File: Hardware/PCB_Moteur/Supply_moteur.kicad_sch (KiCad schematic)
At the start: 26 parts, among them J1 Vin_XT30PW-F, U1 L6981N33DR

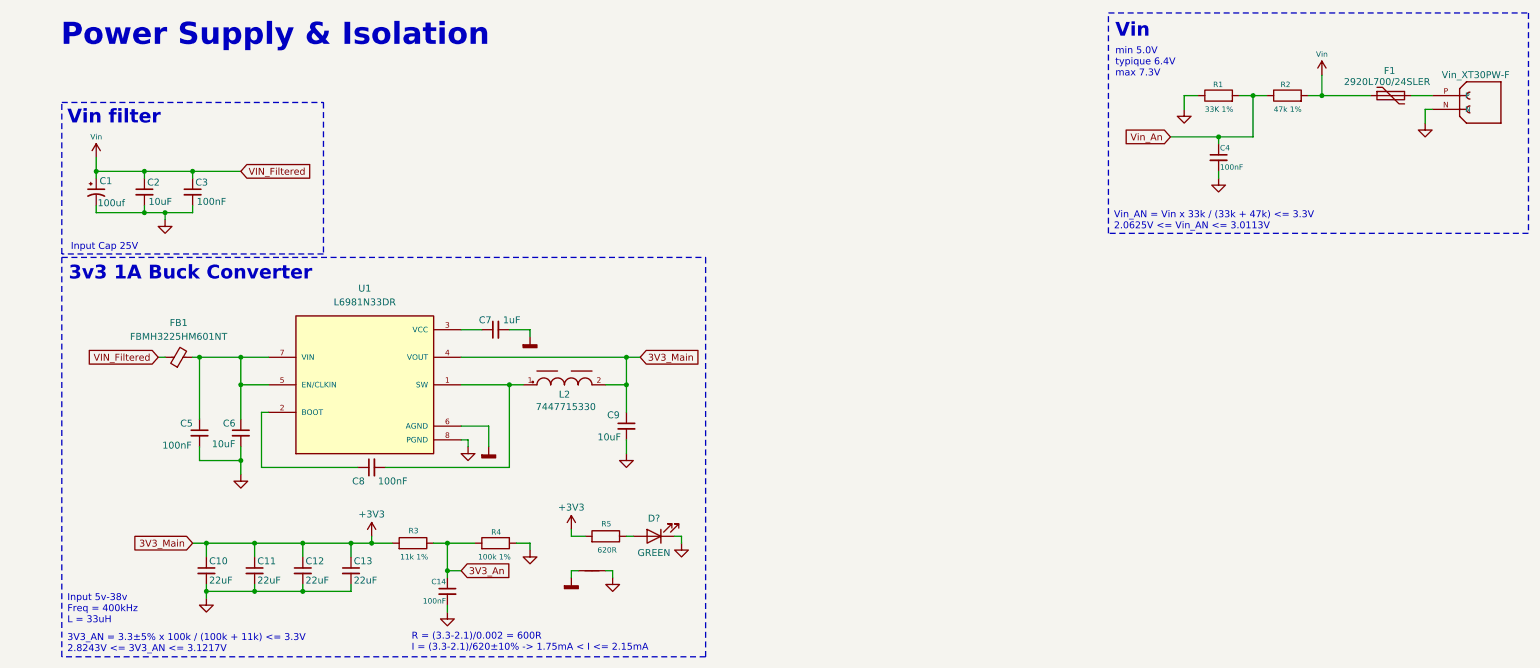
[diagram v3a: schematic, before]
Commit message: fix: symbols refactorisation (footprint missing)
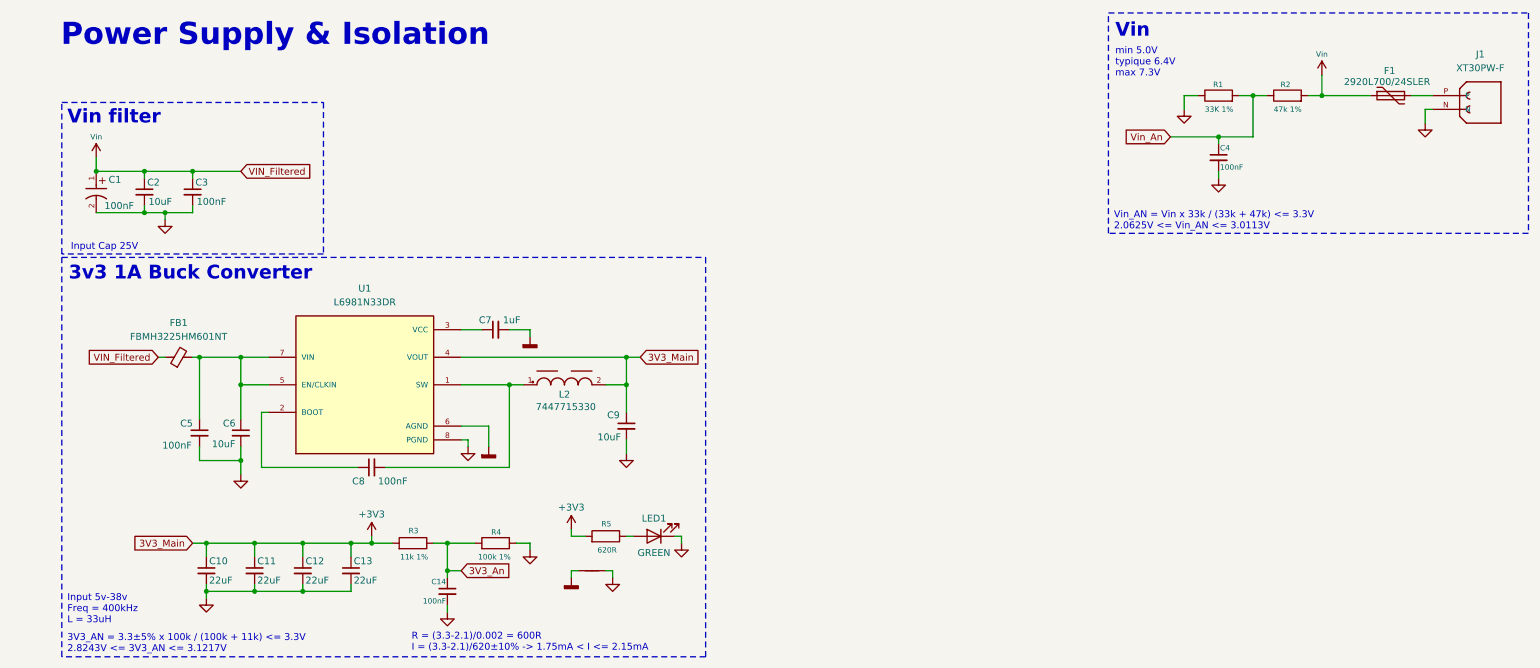
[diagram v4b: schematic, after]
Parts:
- removed C1: 100uf, pcb_moteur:WCAP-PSHP_8X8.7_DXL_, symbol ODB2:875115652007
- removed J1: Vin_XT30PW-F, ODB:AMASS_XT30PW-F, symbol ODB2:XT30PW-F
- removed U1: L6981N33DR, pcb_moteur:SOIC127P600X175-8N, symbol ODB2:L6981N33DR
- added C1: 100nF, WCAP-PSHP_8X8.7:WCAP-PSHP_8X8.7_DXL_, symbol pcb_moteur:WCAP-PSHP_8X8.7
- added J1: XT30PW-F, XT30PW-F:AMASS_XT30PW-F, symbol pcb_moteur:XT30PW-F
- added U1: L6981N33DR, L6981N33DR:SOIC127P600X175-8N, symbol pcb_moteur:L6981N33DR
- gave numbers to parts that had none: 1
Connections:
- net +3V3: now also U1.4 (VOUT)
- net AGND3V3: now also U1.6 (AGND)
- net GND: now also C1.2, J1.N, U1.8 (PGND)
- net Vin: now also C1.1
- net at C5.1, C6.1, FB1.2: now also U1.5 (EN/CLKIN), U1.7 (VIN)
- net at C7.1: now also U1.3 (VCC)
- net at C8.2, L2.1: now also U1.1 (SW)
- net at F1.2: now also J1.P
- net at C8.1: now also U1.2 (BOOT)

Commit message: wip : done all footprints
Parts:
- C1: value 100nF -> 100uF; footprint WCAP-PSHP_8X8.7:WCAP-PSHP_8X8.7_DXL_ -> Capacitor_SMD:C_0805_2012Metric
- J1: footprint XT30PW-F:AMASS_XT30PW-F -> pcb_moteur:XT30PW-F
- LED1: footprint ODB:LED_QBLP601-AG15 -> pcb_moteur:LED_QBLP601-AG15
- U1: footprint L6981N33DR:SOIC127P600X175-8N -> pcb_moteur:L6981N33DR
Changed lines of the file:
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@@
 			)
 		)
-		(property "Footprint" "ODB:LED_QBLP601-AG15"
+		(property "Footprint" "pcb_moteur:LED_QBLP601-AG15"
 			(at 123.19 109.22 0)
 			(effects
@@
 			)
 		)
-		(property "Footprint" "XT30PW-F:AMASS_XT30PW-F"
+		(property "Footprint" "pcb_moteur:XT30PW-F"
 			(at 271.78 27.94 0)
 			(effects
@@
 			)
 		)
-		(property "Value" "100nF"
+		(property "Value" "100uF"
 			(at 21.844 48.26 90)
 			(effects
@@
 			)
 		)
-		(property "Footprint" "WCAP-PSHP_8X8.7:WCAP-PSHP_8X8.7_DXL_"
+		(property "Footprint" "Capacitor_SMD:C_0805_2012Metric"
 			(at 20.32 46.99 0)
 			(effects
@@
 			)
 		)
-		(property "Footprint" "L6981N33DR:SOIC127P600X175-8N"
+		(property "Footprint" "pcb_moteur:L6981N33DR"
 			(at 69.85 81.28 0)
 			(effects

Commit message: début alim
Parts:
- C1: footprint Capacitor_SMD:C_0805_2012Metric -> Capacitor_THT:CP_Radial_D6.3mm_P2.50mm
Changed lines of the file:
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@@
 			)
 		)
-		(property "Footprint" "Capacitor_SMD:C_0805_2012Metric"
+		(property "Footprint" "Capacitor_THT:CP_Radial_D6.3mm_P2.50mm"
 			(at 20.32 46.99 0)
 			(effects

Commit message: wip: layout circuits Pyro
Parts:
- R1, R2, R3, R4, R5: footprint Resistor_SMD:R_0603_1608Metric -> Resistor_SMD:R_0805_2012Metric
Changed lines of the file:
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@@
 			)
 		)
-		(property "Footprint" "Resistor_SMD:R_0603_1608Metric"
+		(property "Footprint" "Resistor_SMD:R_0805_2012Metric"
 			(at 93.98 112.268 90)
 			(effects
@@
 			)
 		)
-		(property "Footprint" "Resistor_SMD:R_0603_1608Metric"
+		(property "Footprint" "Resistor_SMD:R_0805_2012Metric"
 			(at 78.74 112.268 90)
 			(effects
@@
 			)
 		)
-		(property "Footprint" "Resistor_SMD:R_0603_1608Metric"
+		(property "Footprint" "Resistor_SMD:R_0805_2012Metric"
 			(at 114.3 110.998 90)
 			(effects
@@
 			)
 		)
-		(property "Footprint" "Resistor_SMD:R_0603_1608Metric"
+		(property "Footprint" "Resistor_SMD:R_0805_2012Metric"
 			(at 227.33 29.718 90)
 			(effects
@@
 			)
 		)
-		(property "Footprint" "Resistor_SMD:R_0603_1608Metric"
+		(property "Footprint" "Resistor_SMD:R_0805_2012Metric"
 			(at 240.03 29.718 90)
 			(effects

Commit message: wip: fin des circuits sauf ceux du STM
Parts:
- C10, C11, C12, C13: footprint Capacitor_SMD:C_1210_3225Metric -> Capacitor_SMD:C_0805_2012Metric
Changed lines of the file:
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@@
 			)
 		)
-		(property "Footprint" "Capacitor_SMD:C_1210_3225Metric"
+		(property "Footprint" "Capacitor_SMD:C_0805_2012Metric"
 			(at 49.53 115.57 0)
 			(effects
@@
 			)
 		)
-		(property "Footprint" "Capacitor_SMD:C_1210_3225Metric"
+		(property "Footprint" "Capacitor_SMD:C_0805_2012Metric"
 			(at 40.64 115.57 0)
 			(effects
@@
 			)
 		)
-		(property "Footprint" "Capacitor_SMD:C_1210_3225Metric"
+		(property "Footprint" "Capacitor_SMD:C_0805_2012Metric"
 			(at 58.42 115.57 0)
 			(effects
@@
 			)
 		)
-		(property "Footprint" "Capacitor_SMD:C_1210_3225Metric"
+		(property "Footprint" "Capacitor_SMD:C_0805_2012Metric"
 			(at 67.31 115.57 0)
 			(effects
